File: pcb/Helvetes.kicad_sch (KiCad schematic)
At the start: 7 parts

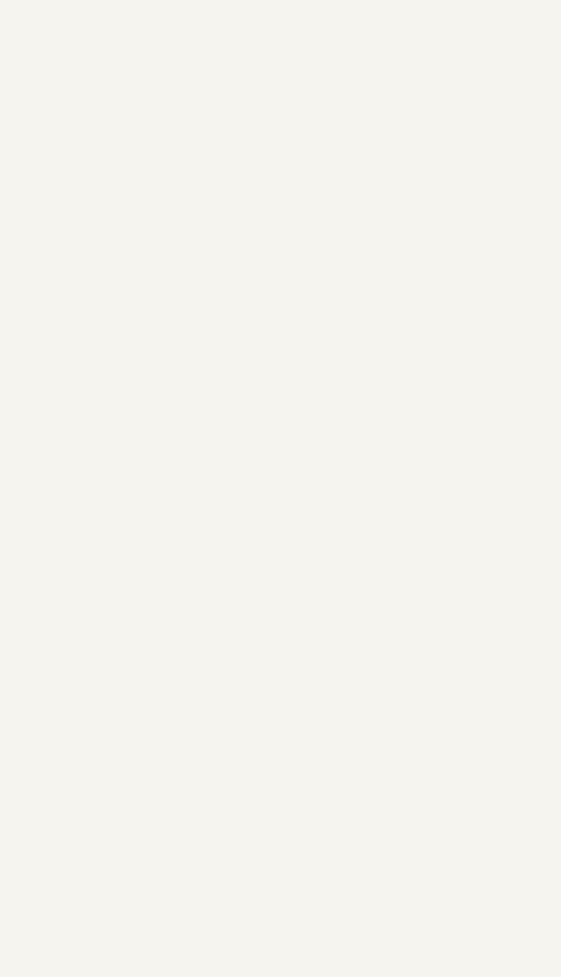
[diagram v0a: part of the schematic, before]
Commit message: :construction: Add the ESP32-S2-WROOM as an MCU component
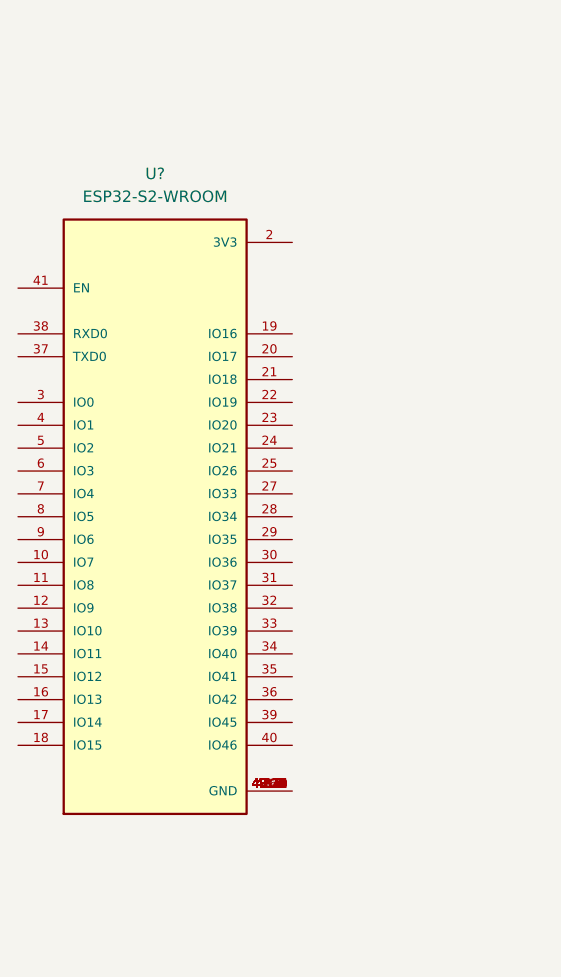
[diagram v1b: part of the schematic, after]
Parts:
- added U?: ESP32-S2-WROOM, XCVR_ESP32-S2-WROOM, symbol ESP32-S2-WROOM:ESP32-S2-WROOM
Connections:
- new net: U?.1 (GND), U?.26 (GND), U?.42 (GND), U?.43.1 (GND), U?.43.10 (GND), U?.43.11 (GND), U?.43.12 (GND), U?.43.13 (GND), U?.43.14 (GND), U?.43.15 (GND), U?.43.16 (GND), U?.43.17 (GND), U?.43.18 (GND), U?.43.19 (GND), U?.43.2 (GND), U?.43.20 (GND), U?.43.21 (GND), U?.43.3 (GND), U?.43.4 (GND), U?.43.5 (GND), U?.43.6 (GND), U?.43.7 (GND), U?.43.8 (GND), U?.43.9 (GND)
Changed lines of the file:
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@@
     (pin "1")
+  )
+  (symbol (lib_id "ESP32-S2-WROOM:ESP32-S2-WROOM") (at 60.96 82.55 0) (unit 1)
+    (in_bom yes) (on_board yes) (fields_autoplaced)
+    (property "Reference" "U?" (id 0) (at 60.96 44.45 0))
+    (property "Value" "ESP32-S2-WROOM" (id 1) (at 60.96 46.99 0))
+    (property "Footprint" "XCVR_ESP32-S2-WROOM" (id 2) (at 60.96 82.55 0)
+      (effects (font (size 1.27 1.27)) (justify left bottom) hide)
+    )
+    (property "Datasheet" "" (id 3) (at 60.96 82.55 0)
+      (effects (font (size 1.27 1.27)) (justify left bottom) hide)
+    )
+    (property "MANUFACTURER" "Espressif Systems" (id 4) (at 60.96 82.55 0)
+      (effects (font (size 1.27 1.27)) (justify left bottom) hide)
+    )
+    (property "PARTREV" "V1.0" (id 5) (at 60.96 82.55 0)
+      (effects (font (size 1.27 1.27)) (justify left bottom) hide)
+    )
+    (property "MAXIMUM_PACKAGE_HEIGHT" "3.45mm" (id 6) (at 60.96 82.55 0)
+      (effects (font (size 1.27 1.27)) (justify left bottom) hide)
+    )
+    (property "STANDARD" "Manufacturer Recommendations" (id 7) (at 60.96 82.55 0)
+      (effects (font (size 1.27 1.27)) (justify left bottom) hide)
+    )
+    (pin "1")
+    (pin "10")
+    (pin "11")
+    (pin "12")
+    (pin "13")
+    (pin "14")
+    (pin "15")
+    (pin "16")
+    (pin "17")
+    (pin "18")
+    (pin "19")
+    (pin "2")
+    (pin "20")
+    (pin "21")
+    (pin "22")
+    (pin "23")
+    (pin "24")
+    (pin "25")
+    (pin "26")
+    (pin "27")
+    (pin "28")
+    (pin "29")
+    (pin "3")
+    (pin "30")
+    (pin "31")
+    (pin "32")
+    (pin "33")
+    (pin "34")
+    (pin "35")
+    (pin "36")
+    (pin "37")
+    (pin "38")
+    (pin "39")
+    (pin "4")
+    (pin "40")
+    (pin "41")
+    (pin "42")
+    (pin "43.1")
+    (pin "43.10")
+    (pin "43.11")
+    (pin "43.12")
+    (pin "43.13")
+    (pin "43.14")
+    (pin "43.15")
+    (pin "43.16")
+    (pin "43.17")
+    (pin "43.18")
+    (pin "43.19")
+    (pin "43.2")
+    (pin "43.20")
+    (pin "43.21")
+    (pin "43.3")
+    (pin "43.4")
+    (pin "43.5")
+    (pin "43.6")
+    (pin "43.7")
+    (pin "43.8")
+    (pin "43.9")
+    (pin "5")
+    (pin "6")
+    (pin "7")
+    (pin "8")
+    (pin "9")
   )
   (symbol (lib_id "Device:C") (at 245.11 31.75 0) (unit 1)
@@
       (reference "U?") (unit 1) (value "LMT85DCK") (footprint "Package_TO_SOT_SMD:SOT-353_SC-70-5")
     )
+    (path "/46cbe85d-ff47-428e-b187-4ebd50a66e0c"
+      (reference "U?") (unit 1) (value "ESP32-S2-WROOM") (footprint "XCVR_ESP32-S2-WROOM")
+    )
     (path "/9bd3b295-cf9b-4409-8a15-32cee0098743"

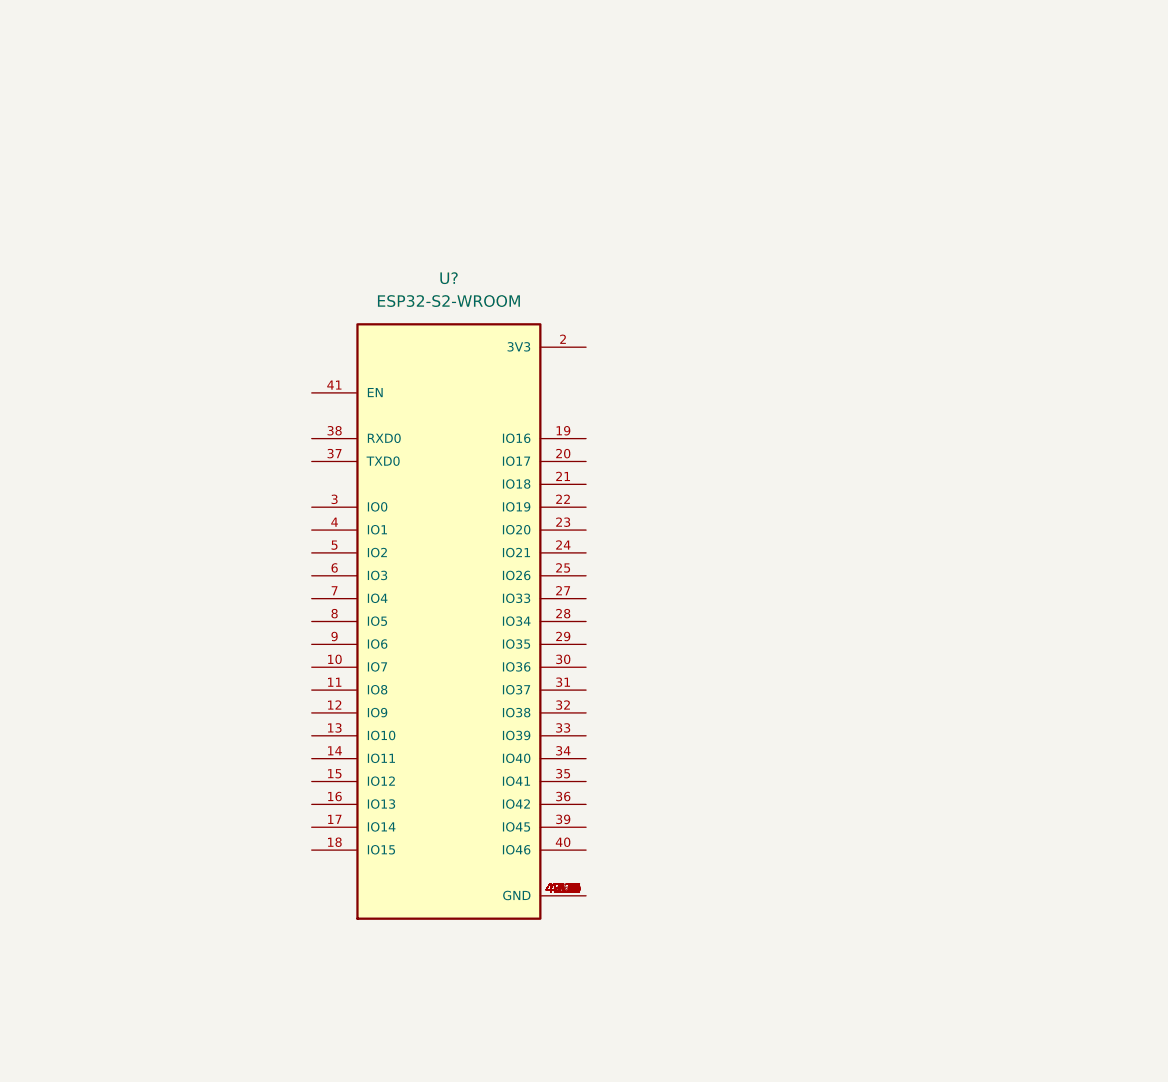
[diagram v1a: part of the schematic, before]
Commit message: :construction: Add the ESP32 to the schematics file
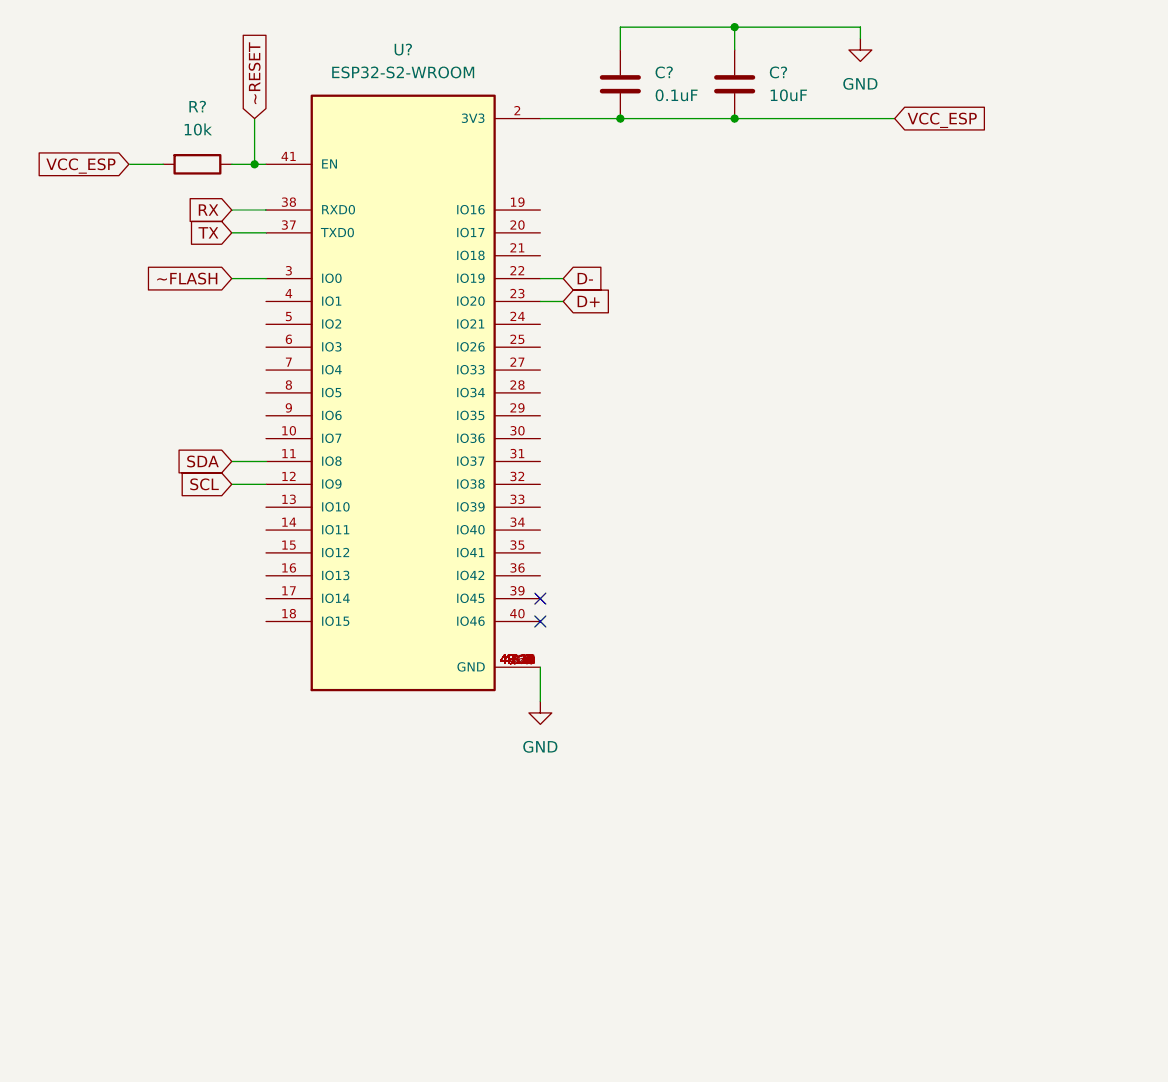
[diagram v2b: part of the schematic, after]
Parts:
- added C?: 0.1uF, symbol Device:C
- added C?: 10uF, symbol Device:C
- added R?: 10k, symbol Device:R
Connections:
- net GND: now also U?.1 (GND), U?.26 (GND), U?.42 (GND), U?.43.1 (GND), U?.43.10 (GND), U?.43.11 (GND), U?.43.12 (GND), U?.43.13 (GND), U?.43.14 (GND), U?.43.15 (GND), U?.43.16 (GND), U?.43.17 (GND), U?.43.18 (GND), U?.43.19 (GND), U?.43.2 (GND), U?.43.20 (GND), U?.43.21 (GND), U?.43.3 (GND), U?.43.4 (GND), U?.43.5 (GND), U?.43.6 (GND), U?.43.7 (GND), U?.43.8 (GND), U?.43.9 (GND), C?.1, C?.1
- net SDA: now reaches U?.11 (IO8)
- net SCL: now reaches U?.12 (IO9)
- net VCC_ESP: now reaches U?.2 (3V3)
- net VCC_ESP: now also C?.2, C?.2, R?.2
- net D-: now reaches U?.22 (IO19)
- net D+: now reaches U?.23 (IO20)
- net ~FLASH: now reaches U?.3 (IO0)
- net TX: now reaches U?.37 (TXD0)
- net RX: now reaches U?.38 (RXD0)
- net ~RESET: now reaches U?.41 (EN)
- net ~RESET: now also R?.1
- no-connect marks 0 -> 2
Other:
- moved on the sheet: U?

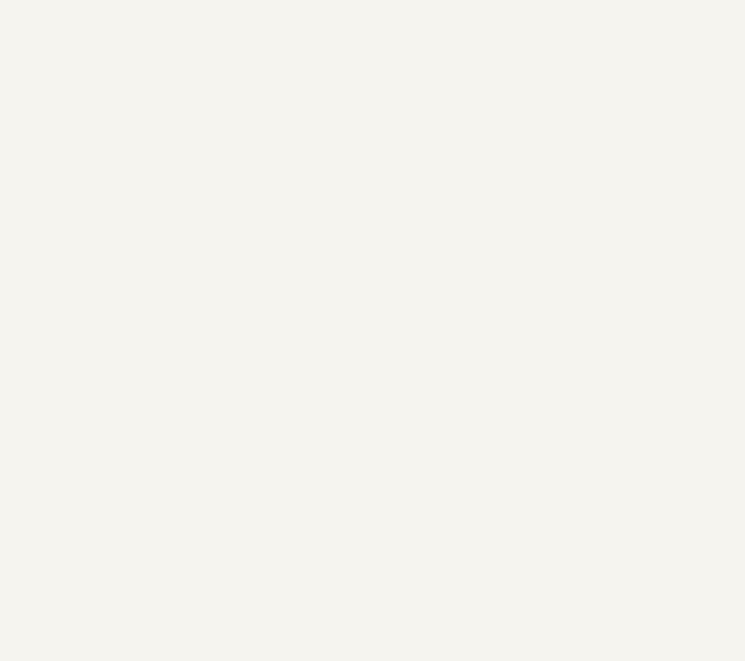
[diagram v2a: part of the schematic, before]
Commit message: :construction: Add a USB-C connector to the schematic
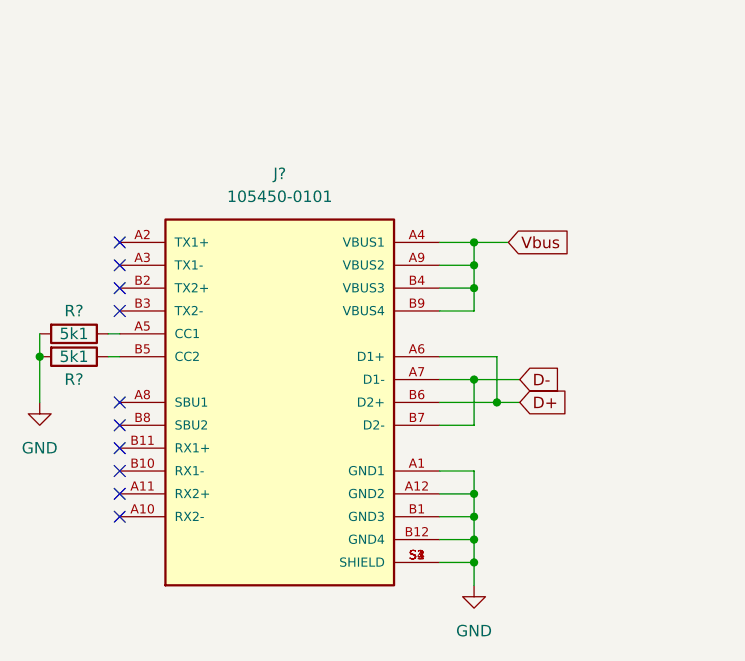
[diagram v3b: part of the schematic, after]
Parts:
- added J?: 105450-0101, MOLEX_105450-0101, symbol 105450-0101:105450-0101
- added R? (x2): 5k1, symbol Device:R
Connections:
- net D+: now also J?.A6 (D1+), J?.B6 (D2+)
- net D-: now also J?.A7 (D1-), J?.B7 (D2-)
- net GND: now also J?.A1 (GND1), J?.A12 (GND2), J?.B1 (GND3), J?.B12 (GND4), J?.S1 (SHIELD), J?.S2 (SHIELD), J?.S3 (SHIELD), J?.S4 (SHIELD), R?.2, R?.2
- new net: J?.A5 (CC1), R?.1
- new net: J?.B5 (CC2), R?.1
- new net Vbus: J?.A4 (VBUS1), J?.A9 (VBUS2), J?.B4 (VBUS3), J?.B9 (VBUS4)
- no-connect marks 2 -> 12

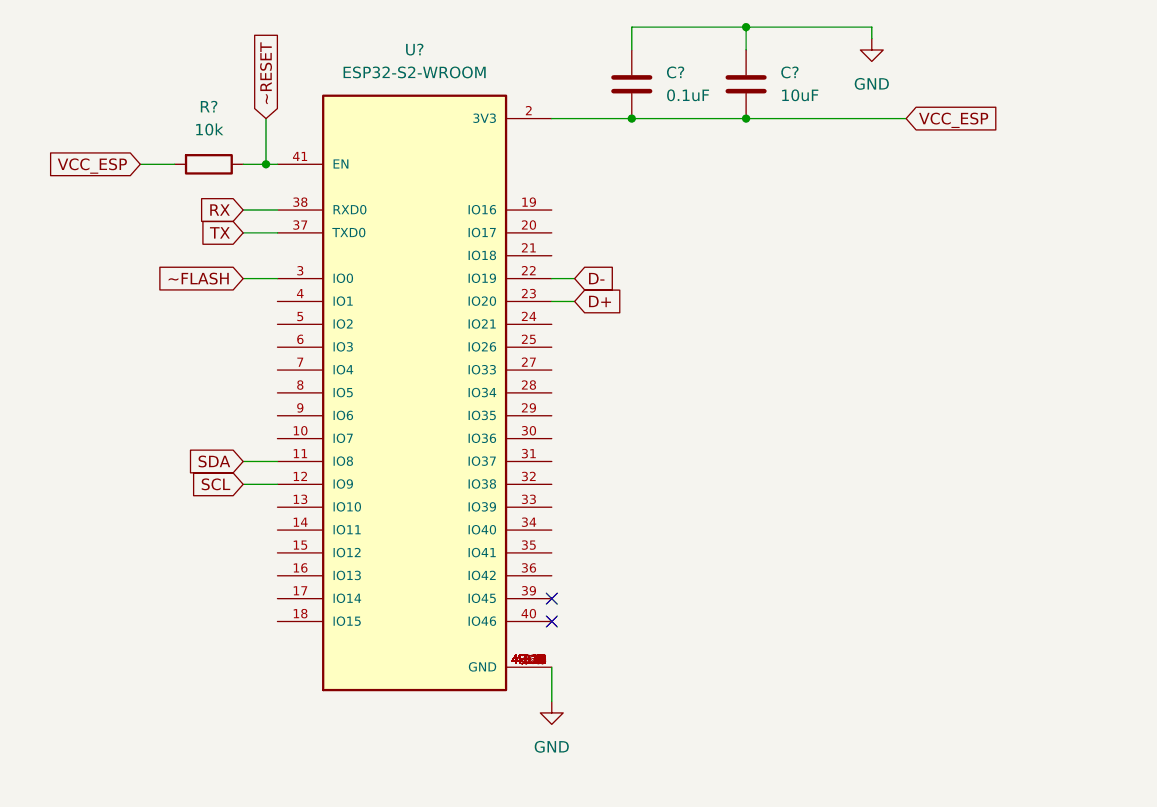
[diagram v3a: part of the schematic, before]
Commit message: :construction: Add two switches for resetting and flashing the ESP
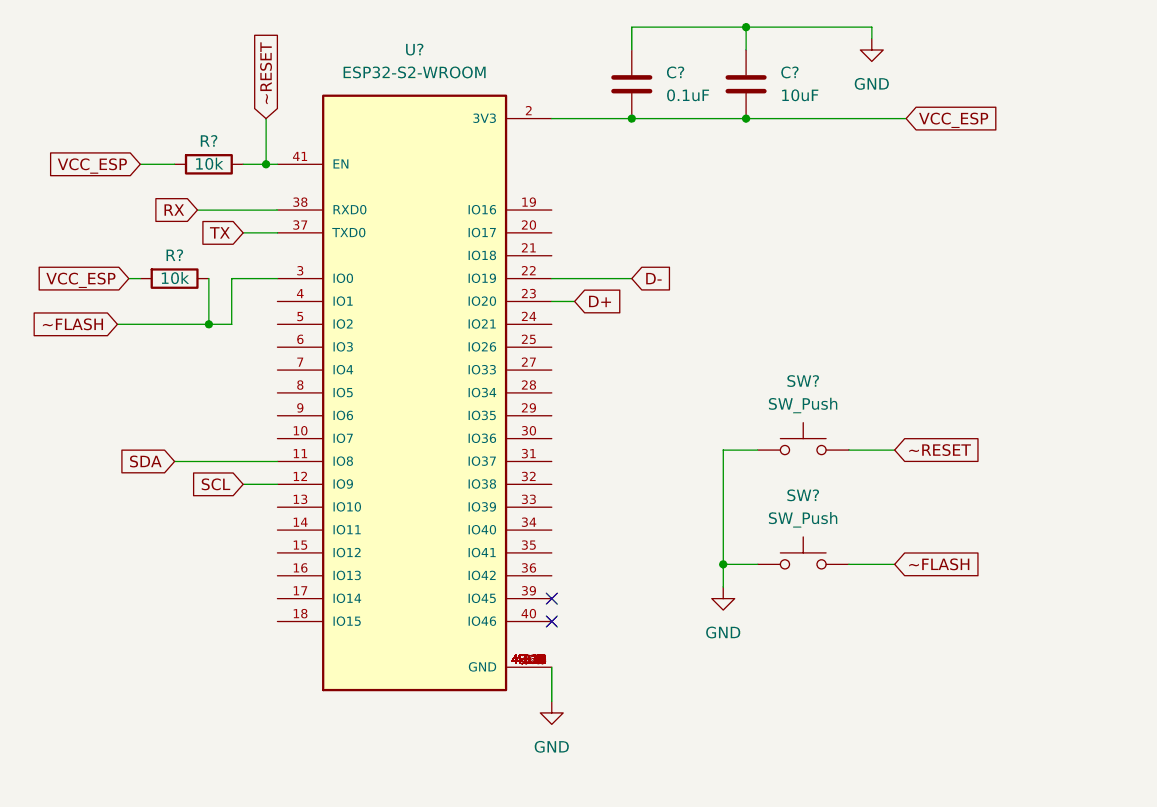
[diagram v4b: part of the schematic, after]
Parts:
- added R?: 10k, symbol Device:R
- added SW? (x2): SW_Push, symbol Switch:SW_Push
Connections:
- net GND: now also SW?.1, SW?.1
- net VCC_ESP: now also R?.2
- net ~FLASH: now also R?.1, SW?.2
- net ~RESET: now also SW?.2
